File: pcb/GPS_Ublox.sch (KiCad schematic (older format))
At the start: 5 parts, among them IC2 u-blox_CAM-M8Q

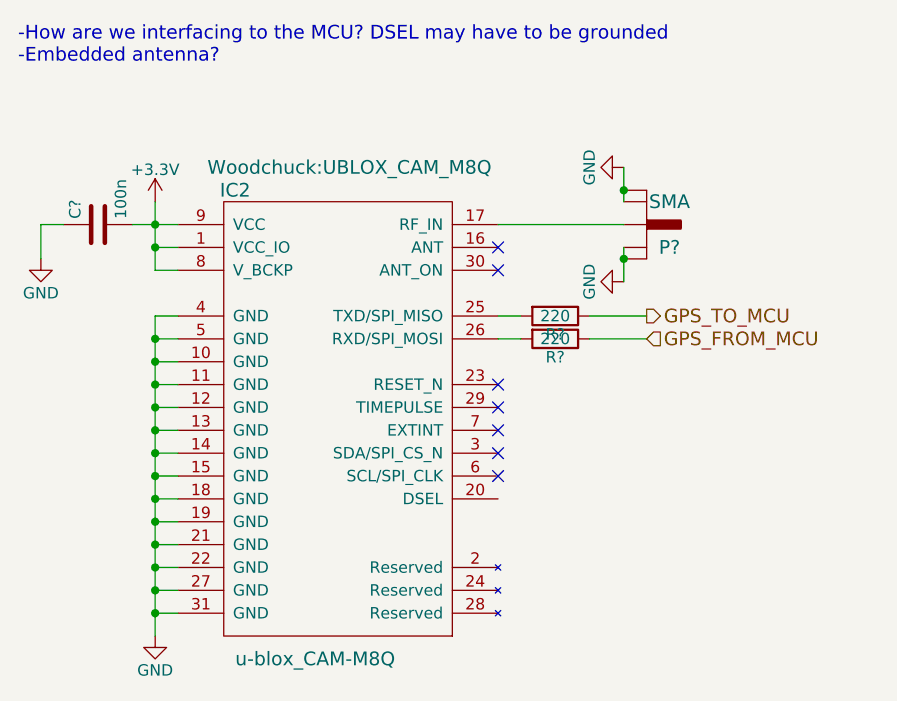
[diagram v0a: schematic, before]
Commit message: Generated net list (only two footprints remaining), added a few footprints, started rough estimate of PCB size
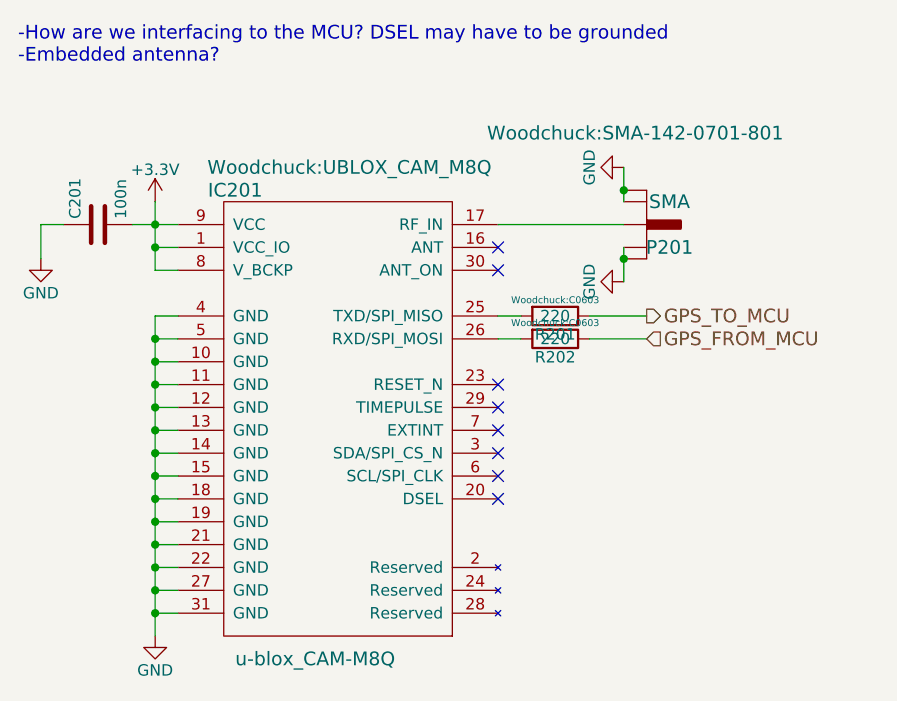
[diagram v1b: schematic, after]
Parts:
- P201: renamed from P?; footprint (none) -> Woodchuck:SMA-142-0701-801
- R201, R202: renamed from R?; footprint (none) -> Woodchuck:C0603
- gave numbers to parts that had none: 1
- renumbered IC2 to IC201
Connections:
- no-connect marks 7 -> 8
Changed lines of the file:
@@
 $EndDescr
 $Comp
-L u-blox_CAM-M8Q IC2
+L u-blox_CAM-M8Q IC201
 U 1 1 565D0659
 P 5350 2900
-F 0 "IC2" H 4900 3450 60  0000 C CNN
+F 0 "IC201" H 4900 3450 60  0000 C CNN
 F 1 "u-blox_CAM-M8Q" H 5250 1400 60  0000 C CNN
 F 2 "Woodchuck:UBLOX_CAM_M8Q" H 5400 3550 60  0000 C CNN
@@
 $EndComp
 $Comp
-L GND #PWR?
+L GND #PWR05
 U 1 1 56AAB217
 P 4550 4300
-F 0 "#PWR?" H 4550 4050 50  0001 C CNN
+F 0 "#PWR05" H 4550 4050 50  0001 C CNN
 F 1 "GND" H 4550 4150 50  0000 C CNN
 F 2 "" H 4550 4300 60  0000 C CNN
@@
 Connection ~ 4550 4100
 $Comp
-L +3.3V #PWR?
+L +3.3V #PWR06
 U 1 1 56AAB35F
 P 4550 2400
-F 0 "#PWR?" H 4550 2250 50  0001 C CNN
+F 0 "#PWR06" H 4550 2250 50  0001 C CNN
 F 1 "+3.3V" H 4550 2540 50  0000 C CNN
 F 2 "" H 4550 2400 60  0000 C CNN
@@
 -How are we interfacing to the MCU? DSEL may have to be grounded\n-Embedded antenna?
 $Comp
-L C C?
+L C C201
 U 1 1 56ACB00C
 P 4300 2500
-F 0 "C?" H 4325 2600 50  0000 L CNN
+F 0 "C201" H 4325 2600 50  0000 L CNN
 F 1 "100n" H 4325 2400 50  0000 L CNN
 F 2 "Woodchuck:C0603" H 4338 2350 30  0001 C CNN
@@
 	4050 2500 4050 2650
 $Comp
-L GND #PWR?
+L GND #PWR07
 U 1 1 56ACB0DE
 P 4050 2650
-F 0 "#PWR?" H 4050 2400 50  0001 C CNN
+F 0 "#PWR07" H 4050 2400 50  0001 C CNN
 F 1 "GND" H 4050 2500 50  0000 C CNN
 F 2 "" H 4050 2650 60  0000 C CNN
@@
 $EndComp
 $Comp
-L SMA P?
+L SMA P201
 U 1 1 56ACB5C4
 P 6700 2500
-F 0 "P?" H 6800 2400 60  0000 C CNN
+F 0 "P201" H 6800 2400 60  0000 C CNN
 F 1 "SMA" H 6800 2600 60  0000 C CNN
-F 2 "" H 6700 2500 60  0000 C CNN
+F 2 "Woodchuck:SMA-142-0701-801" H 6650 2900 60  0000 C CNN
 F 3 "" H 6700 2500 60  0000 C CNN
 	1    6700 2500
@@
 	6600 2500 6050 2500
 $Comp
-L GND #PWR?
+L GND #PWR08
 U 1 1 56ACB7D0
 P 6600 2250
-F 0 "#PWR?" H 6600 2000 50  0001 C CNN
+F 0 "#PWR08" H 6600 2000 50  0001 C CNN
 F 1 "GND" H 6600 2100 50  0000 C CNN
 F 2 "" H 6600 2250 60  0000 C CNN
@@
 $EndComp
 $Comp
-L GND #PWR?
+L GND #PWR09
 U 1 1 56ACB7EA
 P 6600 2750
-F 0 "#PWR?" H 6600 2500 50  0001 C CNN
+F 0 "#PWR09" H 6600 2500 50  0001 C CNN
 F 1 "GND" H 6600 2600 50  0000 C CNN
 F 2 "" H 6600 2750 60  0000 C CNN
@@
 NoConn ~ 6050 2700
 $Comp
-L R R?
+L R R202
 U 1 1 56ACBA41
 P 6300 3000
-F 0 "R?" V 6380 3000 50  0000 C CNN
+F 0 "R202" V 6380 3000 50  0000 C CNN
 F 1 "220" V 6300 3000 50  0000 C CNN
-F 2 "" V 6230 3000 30  0000 C CNN
+F 2 "Woodchuck:C0603" V 6230 3000 30  0000 C CNN
 F 3 "" H 6300 3000 30  0000 C CNN
 	1    6300 3000
@@
 $EndComp
 $Comp
-L R R?
+L R R201
 U 1 1 56ACBA86
 P 6300 2900
-F 0 "R?" V 6380 2900 50  0000 C CNN
+F 0 "R201" V 6380 2900 50  0000 C CNN
 F 1 "220" V 6300 2900 50  0000 C CNN
-F 2 "" V 6230 2900 30  0000 C CNN
+F 2 "Woodchuck:C0603" V 6230 2900 30  0000 C CNN
 F 3 "" H 6300 2900 30  0000 C CNN
 	1    6300 2900
@@
 	4550 2700 4650 2700
 Connection ~ 4550 2600
+NoConn ~ 6050 3700
 $EndSCHEMATC

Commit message: Removed antenna for GPS module, connected ANT to RF-IN
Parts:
- removed P201: SMA, Woodchuck:SMA-142-0701-801, symbol SMA
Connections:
- net at IC201.16 (ANT): now also IC201.17 (RF_IN)
- no-connect marks 8 -> 7
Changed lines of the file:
@@
 	1    0    0    -1
 $EndComp
-$Comp
-L SMA P201
-U 1 1 56ACB5C4
-P 6700 2500
-F 0 "P201" H 6800 2400 60  0000 C CNN
-F 1 "SMA" H 6800 2600 60  0000 C CNN
-F 2 "Woodchuck:SMA-142-0701-801" H 6650 2900 60  0000 C CNN
-F 3 "" H 6700 2500 60  0000 C CNN
-	1    6700 2500
-	1    0    0    -1
-$EndComp
-Wire Wire Line
-	6600 2600 6600 2750
-Connection ~ 6600 2650
-Wire Wire Line
-	6600 2250 6600 2400
-Connection ~ 6600 2350
-Wire Wire Line
-	6600 2500 6050 2500
-$Comp
-L GND #PWR08
-U 1 1 56ACB7D0
-P 6600 2250
-F 0 "#PWR08" H 6600 2000 50  0001 C CNN
-F 1 "GND" H 6600 2100 50  0000 C CNN
-F 2 "" H 6600 2250 60  0000 C CNN
-F 3 "" H 6600 2250 60  0000 C CNN
-	1    6600 2250
-	0    1    1    0
-$EndComp
-$Comp
-L GND #PWR09
-U 1 1 56ACB7EA
-P 6600 2750
-F 0 "#PWR09" H 6600 2500 50  0001 C CNN
-F 1 "GND" H 6600 2600 50  0000 C CNN
-F 2 "" H 6600 2750 60  0000 C CNN
-F 3 "" H 6600 2750 60  0000 C CNN
-	1    6600 2750
-	0    1    1    0
-$EndComp
-NoConn ~ 6050 2600
 NoConn ~ 6050 2700
 $Comp
@@
 Connection ~ 4550 2600
 NoConn ~ 6050 3700
+Wire Wire Line
+	6050 2600 6050 2500
 $EndSCHEMATC

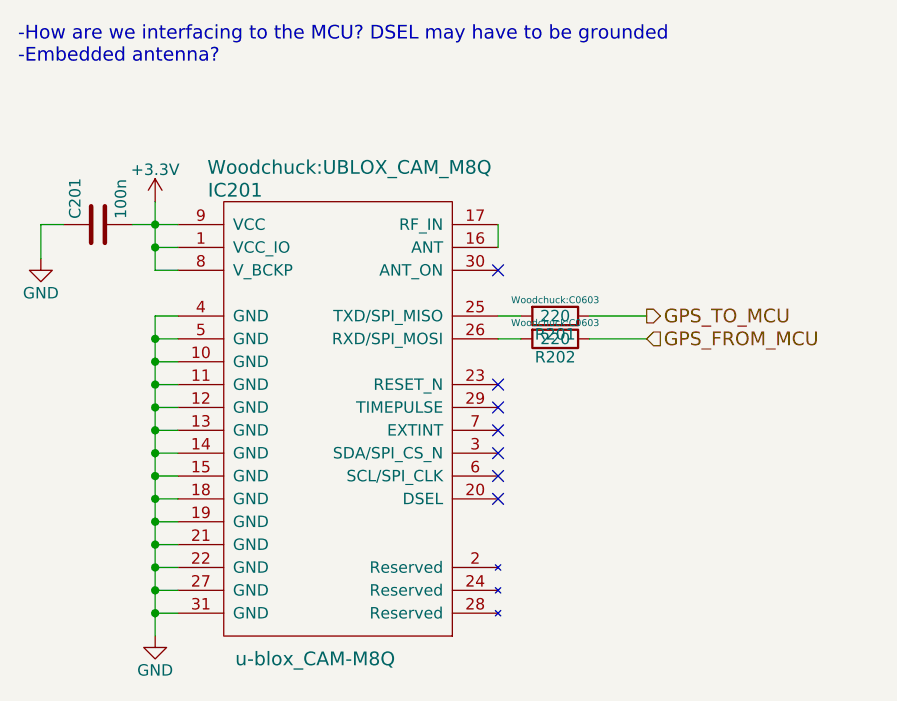
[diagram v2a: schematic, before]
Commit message: Added a footprint and changed footprints for resistors to the 0603 SMD footprint.
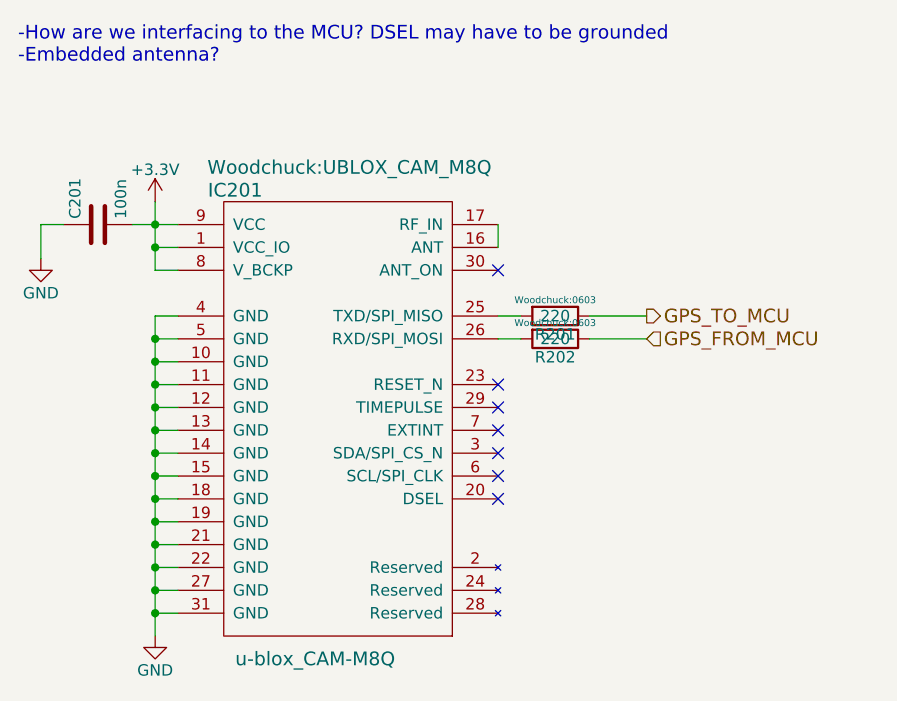
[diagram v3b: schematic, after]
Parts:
- R201, R202: footprint Woodchuck:C0603 -> Woodchuck:0603
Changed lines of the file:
@@
 F 0 "R202" V 6380 3000 50  0000 C CNN
 F 1 "220" V 6300 3000 50  0000 C CNN
-F 2 "Woodchuck:C0603" V 6230 3000 30  0000 C CNN
+F 2 "Woodchuck:0603" V 6230 3000 30  0000 C CNN
 F 3 "" H 6300 3000 30  0000 C CNN
 	1    6300 3000
@@
 F 0 "R201" V 6380 2900 50  0000 C CNN
 F 1 "220" V 6300 2900 50  0000 C CNN
-F 2 "Woodchuck:C0603" V 6230 2900 30  0000 C CNN
+F 2 "Woodchuck:0603" V 6230 2900 30  0000 C CNN
 F 3 "" H 6300 2900 30  0000 C CNN
 	1    6300 2900

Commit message: Fix barometer hierarchical pins and add Farnell numbers to components
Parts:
- R201, R202: Digikey (none) -> Value; Farnell (none) -> 1652857; Fieldname (none) -> Value
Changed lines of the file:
@@
 F 2 "Woodchuck:0603" V 6230 3000 30  0000 C CNN
 F 3 "" H 6300 3000 30  0000 C CNN
+F 4 "Value" H 6300 3000 60  0001 C CNN "Digikey"
+F 5 "1652857" H 6300 3000 60  0001 C CNN "Farnell"
+F 6 "Value" H 6300 3000 60  0001 C CNN "Fieldname"
 	1    6300 3000
 	0    1    1    0
@@
 F 2 "Woodchuck:0603" V 6230 2900 30  0000 C CNN
 F 3 "" H 6300 2900 30  0000 C CNN
+F 4 "Value" H 6300 2900 60  0001 C CNN "Digikey"
+F 5 "1652857" H 6300 2900 60  0001 C CNN "Farnell"
+F 6 "Value" H 6300 2900 60  0001 C CNN "Fieldname"
 	1    6300 2900
 	0    1    1    0

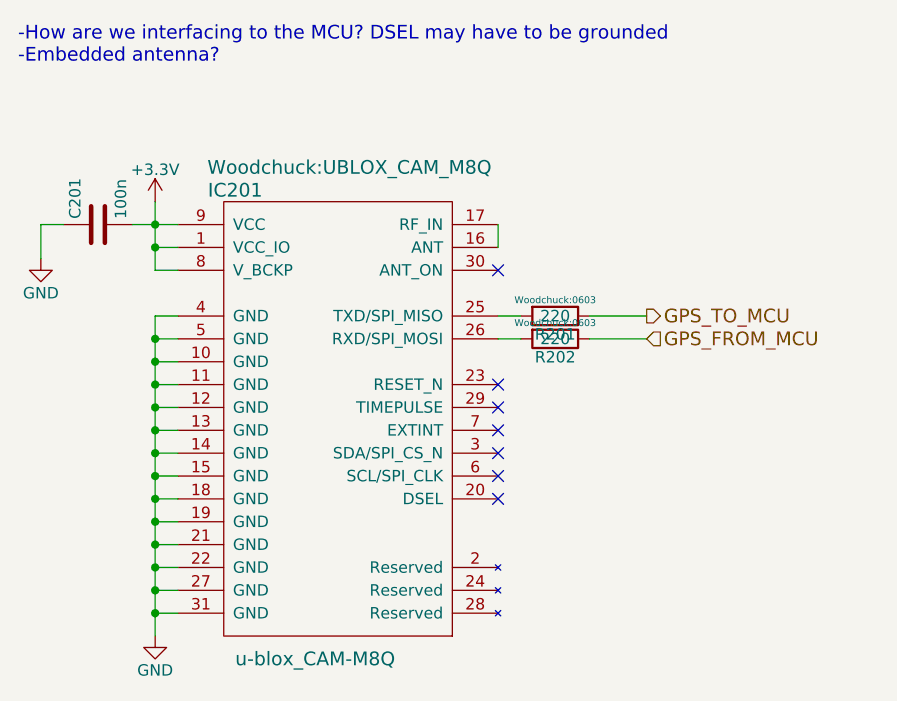
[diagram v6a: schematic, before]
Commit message: Worked on PCB layout
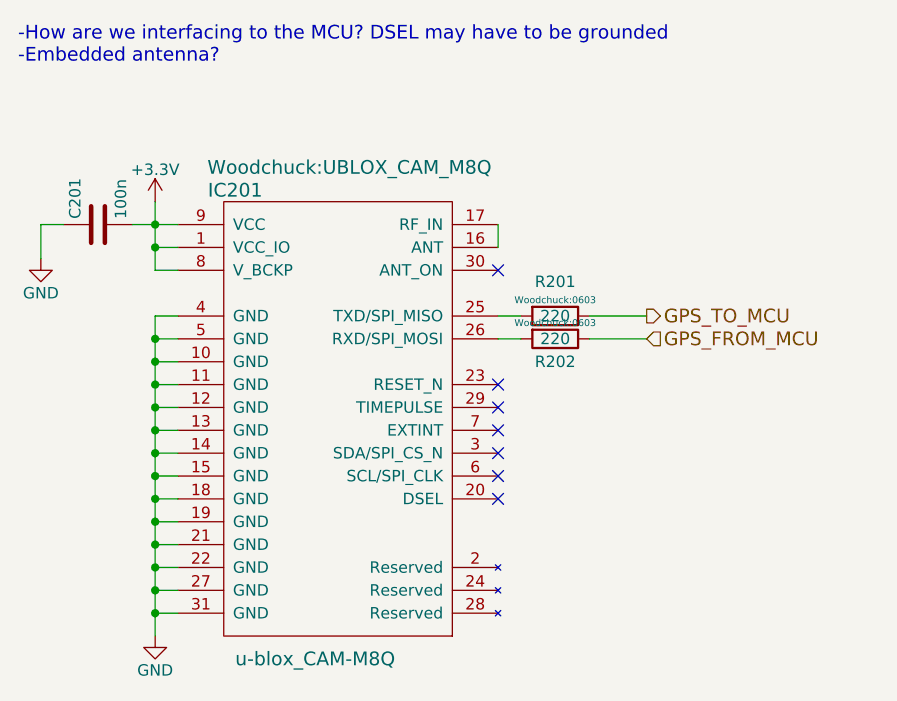
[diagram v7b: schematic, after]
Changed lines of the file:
@@
 U 1 1 56ACBA41
 P 6300 3000
-F 0 "R202" V 6380 3000 50  0000 C CNN
+F 0 "R202" V 6400 3000 50  0000 C CNN
 F 1 "220" V 6300 3000 50  0000 C CNN
 F 2 "Woodchuck:0603" V 6230 3000 30  0000 C CNN
@@
 U 1 1 56ACBA86
 P 6300 2900
-F 0 "R201" V 6380 2900 50  0000 C CNN
+F 0 "R201" V 6150 2900 50  0000 C CNN
 F 1 "220" V 6300 2900 50  0000 C CNN
 F 2 "Woodchuck:0603" V 6230 2900 30  0000 C CNN
